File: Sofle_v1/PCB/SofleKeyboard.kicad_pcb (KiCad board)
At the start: 2 copper layers, 137.2 x 109.2 mm, 93 parts, among them J1 LED, J2 4PIN, J3 OLED, P1 i2c_pin, P2 i2c_pin, SW1 SW_PUSH, SW10 SW_PUSH, SW11 SW_PUSH, SW12 SW_PUSH, SW13 SW_PUSH, SW14 SW_PUSH, SW15 SW_PUSH, SW16 SW_PUSH, SW17 SW_PUSH, SW18 SW_PUSH, SW19 SW_PUSH, SW2 SW_PUSH, SW20 SW_PUSH, SW21 SW_PUSH, SW22 SW_PUSH, SW23 SW_PUSH, SW24 SW_PUSH, SW25 Rotary_Encoder_Switch, SW26 SW_PUSH, SW27 SW_PUSH, SW28 SW_PUSH, SW29 SW_PUSH, SW3 SW_PUSH, SW30 SW_PUSH, SW31 SW_PUSH, SW4 SW_PUSH, SW5 SW_PUSH, SW6 SW_PUSH, SW7 SW_PUSH, SW8 SW_PUSH, SW9 SW_PUSH, U1 ProMicro

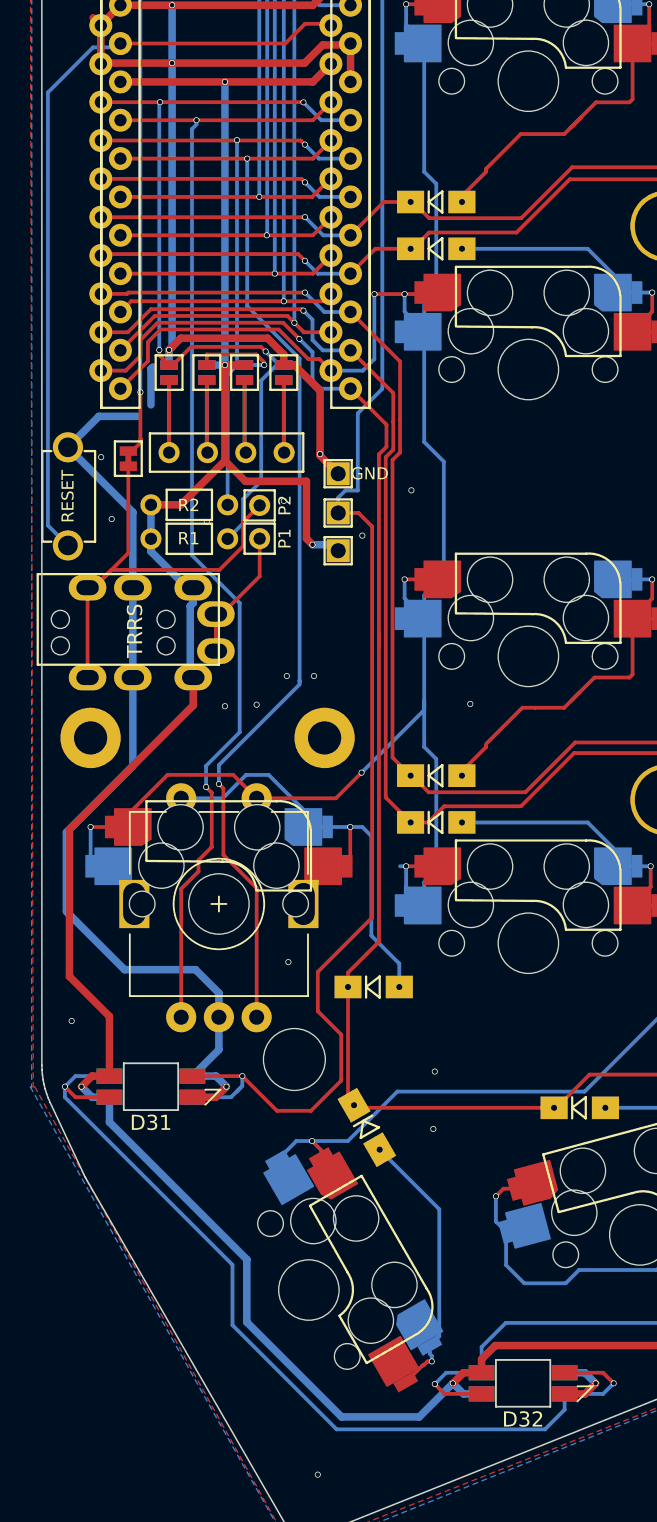
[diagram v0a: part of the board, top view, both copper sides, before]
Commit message: Fixed the mounting holes
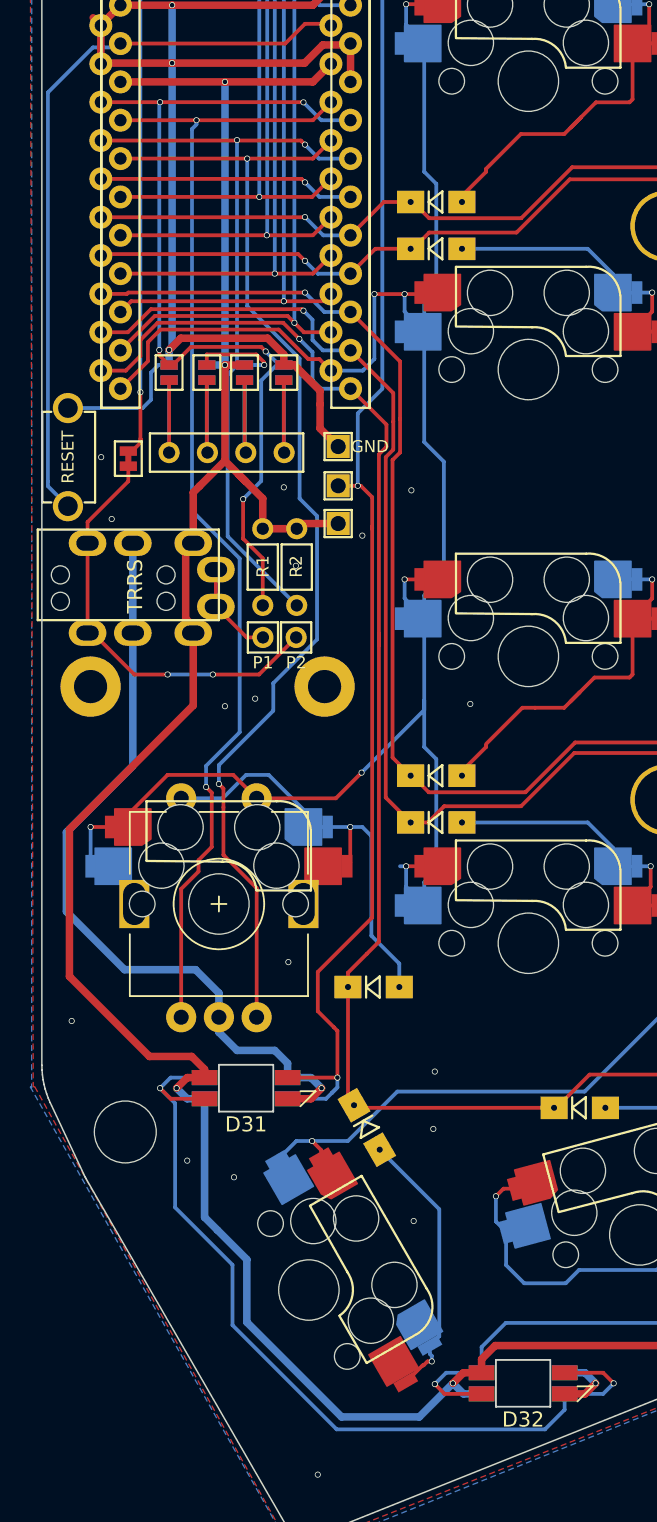
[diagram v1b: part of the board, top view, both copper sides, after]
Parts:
- moved TH7 12.2 mm to (93.8, 119.6)
- moved P2 9.07 mm to (105.1, 86.8), turned to 180 degrees
- moved R2 8.22 mm to (105.2, 82.2), turned to 270 degrees
- moved P1 6.55 mm to (102.9, 86.8), turned to 180 degrees
- moved D31 6.30 mm to (101.8, 116.7)
- moved R1 5.21 mm to (102.9, 82.2), turned to 270 degrees
- moved TH1 3.40 mm to (91.5, 90.1)
- moved TH2 3.40 mm to (107.0, 90.1)
- moved J2 2.95 mm to (88.0, 82.7)
- moved RSW1 2.60 mm to (90.0, 74.9)
- moved J1 1.80 mm to (107.9, 79.3)
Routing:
- net LED: track 113.5 -> 104.1 mm, vias 2 -> 3
- net SCL: track 50.1 -> 58.7 mm
- net GND: track 176.3 -> 168.8 mm
- net SDA: track 57.0 -> 61.5 mm, vias 4 -> 5
- net VCC: track 368.9 -> 365.5 mm, vias 13 -> 12
- net Net-(D31-Pad2): track 60.4 -> 57.7 mm
- net /i2c_c: track 9.85 -> 7.21 mm
- net RESET: track 51.2 -> 48.6 mm
- net /i2c_d: track 29.6 -> 28.1 mm, vias 0 -> 2
- net ENCB: track 76.1 -> 77.0 mm
